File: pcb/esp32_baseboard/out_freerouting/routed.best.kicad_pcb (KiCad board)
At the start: 2 copper layers, 235 x 132 mm, 39 parts, among them J1 Screw_12V_IN, J10 LIM_HOME2, J12 LIM_HOME3, J14 BUP_30S, J15 BUZZER_5V, J16 AOD4184, J17 TFT_TOUCH, J18 EC11_ENC, J2 NEMA17_OUT, J5 28BYJ48, J6 28BYJ48, J7 28BYJ48, J8 LIM_HOME1, U1 ESP32_S3_DevKitC_1, U10 74HC595, U11 74HC595, U2 MP1584_5V3A, U3 TMC2209, U4 PC817_4CH, U5 ULN2003AN, U6 ULN2003AN, U7 ULN2003AN, U9 PC817_4CH_DNP

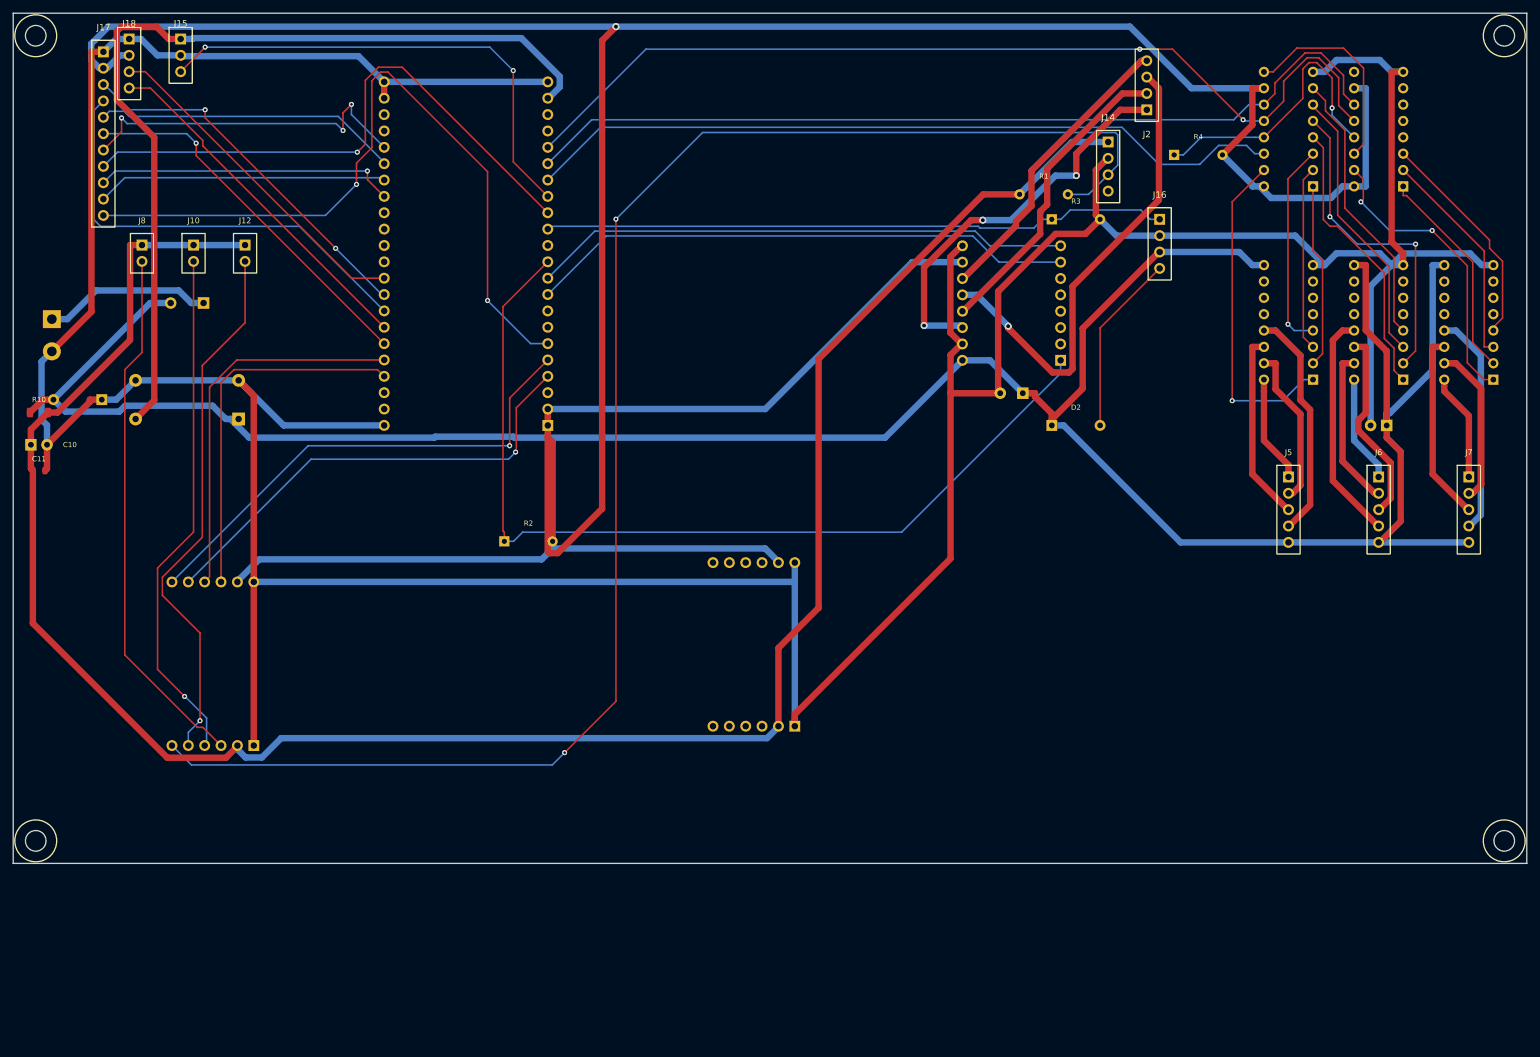
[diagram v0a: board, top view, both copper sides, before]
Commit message: đi dây cho mạch PCB
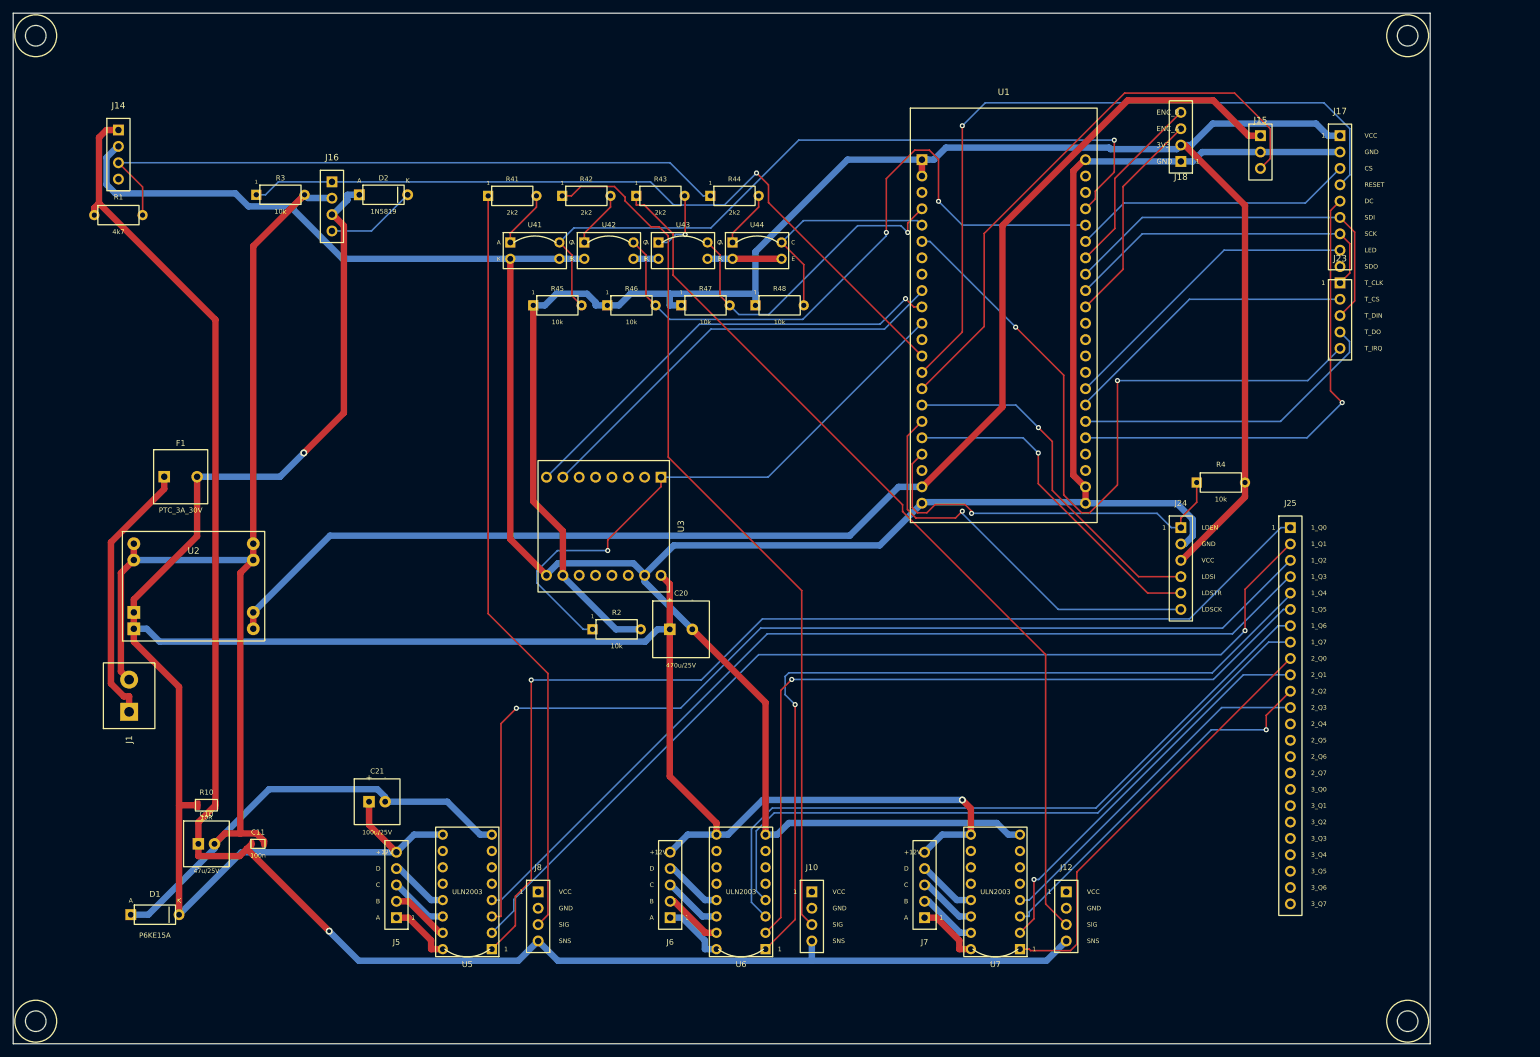
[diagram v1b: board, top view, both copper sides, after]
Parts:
- removed J2: NEMA17_OUT, ESP32_Carrier:PinHeader_1x04_Motor
- removed U10, U11: 74HC595, ESP32_Carrier:74HC595
- removed U4: PC817_4CH, ESP32_Carrier:PC817_4CH_Opto
- removed U9: PC817_4CH_DNP, ESP32_Carrier:PC817_4CH_Opto
- added J23: TFT_TP, ESP32_Carrier:PinHeader_1x05_TFT_TP, F.Cu at (241.0, 71.9)
- added J24: 595_CTRL, ESP32_Carrier:PinHeader_1x06_595CTRL, F.Cu at (216.3, 109.9)
- added J25: 595_Q, ESP32_Carrier:PinHeader_1x24_595Q, F.Cu at (233.3, 109.9)
- added R41: 2k2, ESP32_Carrier:R_Axial_4k7_BUP, F.Cu at (112.5, 58.4)
- added R42: 2k2, ESP32_Carrier:R_Axial_4k7_BUP, F.Cu at (124.0, 58.4)
- added R43: 2k2, ESP32_Carrier:R_Axial_4k7_BUP, F.Cu at (135.5, 58.4)
- added R44: 2k2, ESP32_Carrier:R_Axial_4k7_BUP, F.Cu at (147.0, 58.4)
- added R45: 10k, ESP32_Carrier:R_Axial_4k7_BUP, F.Cu at (119.5, 75.4)
- added R46: 10k, ESP32_Carrier:R_Axial_4k7_BUP, F.Cu at (131.0, 75.4)
- added R47: 10k, ESP32_Carrier:R_Axial_4k7_BUP, F.Cu at (142.5, 75.4)
- added R48: 10k, ESP32_Carrier:R_Axial_4k7_BUP, F.Cu at (154.0, 75.4)
- added U41: PC817, ESP32_Carrier:PC817_DIP4, F.Cu at (116.0, 66.9)
- added U42: PC817, ESP32_Carrier:PC817_DIP4, F.Cu at (127.5, 66.9)
- added U43: PC817, ESP32_Carrier:PC817_DIP4, F.Cu at (139.0, 66.9)
- added U44: PC817, ESP32_Carrier:PC817_DIP4, F.Cu at (150.5, 66.9)
- C20, C21, D1, F1, J1, U1, U2, U3, U5, U6, U7: moved to F.Cu
- J10: value LIM_HOME2 -> END_HOME2; footprint ESP32_Carrier:PinHeader_1x02_LimitSW -> ESP32_Carrier:PinHeader_1x04_Endstop
- J12: value LIM_HOME3 -> END_HOME3; footprint ESP32_Carrier:PinHeader_1x02_LimitSW -> ESP32_Carrier:PinHeader_1x04_Endstop
- J17: value TFT_TOUCH -> TFT_LCD; footprint ESP32_Carrier:PinHeader_1x11_TFT -> ESP32_Carrier:PinHeader_1x09_TFT_LCD
- J8: value LIM_HOME1 -> END_HOME1; footprint ESP32_Carrier:PinHeader_1x02_LimitSW -> ESP32_Carrier:PinHeader_1x04_Endstop
- moved J17 192.4 mm to (241.0, 49.0)
- moved J15 168.3 mm to (228.6, 49.0)
- moved C21 166.1 mm to (91.5, 152.4), turned to 0 degrees
- moved J18 164.4 mm to (216.3, 53.0), turned to 180 degrees
- moved J12 162.3 mm to (198.5, 166.4)
- moved U5 155.2 mm to (105.5, 166.4)
- moved J5 154.5 mm to (94.5, 170.4), turned to 180 degrees
- moved J14 153.7 mm to (51.3, 48.1)
- moved R1 143.7 mm to (51.3, 61.3)
- moved J10 138.9 mm to (159.0, 166.4)
- moved U6 132.7 mm to (148.0, 166.4)
- moved J6 129.5 mm to (137.0, 170.4), turned to 180 degrees
- moved J16 128.6 mm to (84.5, 56.2)
- moved R3 123.6 mm to (76.5, 58.2)
- moved J8 117.8 mm to (116.5, 166.4)
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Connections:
- J10 pad 1: +12V_SNS -> unconnected-(J10-VCC-Pad1)
- J10 pad 2: OPTO_IN2 -> unconnected-(J10-GND-Pad2)
- J12 pad 1: +12V_SNS -> unconnected-(J12-VCC-Pad1)
- J12 pad 2: OPTO_IN3 -> unconnected-(J12-GND-Pad2)
- J17 pad 1: GND -> +3V3
- J17 pad 2: +3V3 -> GND
- J17 pad 3: TFT_SCK -> TFT_CS
- J17 pad 4: TFT_MOSI -> TFT_RST
- J17 pad 5: TFT_MISO -> TFT_DC
- J17 pad 6: TFT_CS -> TFT_MOSI
- J17 pad 7: TFT_DC -> TFT_SCK
- J17 pad 8: TFT_RST -> TFT_BL
- J17 pad 9: TFT_BL -> unconnected-(J17-SDO-Pad9)
- J8 pad 1: +12V_SNS -> unconnected-(J8-VCC-Pad1)
- J8 pad 2: OPTO_IN1 -> unconnected-(J8-GND-Pad2)
- U2 pad 3: +5V -> GND
- U2 pad 4: GND -> +5V
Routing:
- net +3V3: track 542.4 -> 284.1 mm, vias 1 -> 0
- net OPTO_IN4: track 247.1 -> 103.7 mm, vias 2 -> 0
- net SR_Q2: track 28.7 -> 164.4 mm, vias 0 -> 1
- net SR_Q1: track 28.7 -> 153.8 mm, vias 0 -> 1
- net SR_Q0: track 51.8 -> 172.0 mm
- net SR_Q3: track 32.4 -> 144.8 mm, vias 1 -> 0
- net RCLK: track 148.6 -> 53.0 mm, vias 2 -> 1
- net SR_Q4: track 44.1 -> 128.8 mm, vias 0 -> 1
- net MotB1: track 74.2 -> 0.00 mm, vias 1 -> 0
- net SRCLK: track 138.3 -> 64.6 mm, vias 0 -> 1
- net SR_Q5: track 50.3 -> 122.9 mm, vias 2 -> 1
- net +5V: track 140.4 -> 210.6 mm
- net SR_Q6: track 43.4 -> 111.2 mm
- net SER: track 118.7 -> 55.7 mm, vias 0 -> 1
- net SR_Q7: track 43.4 -> 106.4 mm
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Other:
- board size 235 x 132 mm -> 220 x 160 mm
- board text added: "1: POWER J1+F1+D1+U2+RC"
- board text added: "2: MCU U1 ESP32-S3 DevKitC"
- board text added: "3: TMC U3 + Mot pins (NEMA17 on module)"
- board text added: "4: OPTO U41-U44 PC817 + R2k2/10k"
- board text added: "5: SHIFT U10 595-24IO + J24/J25 + R4"
- board text added: "A1: HOME1+U5+J5"
- board text added: "A2: HOME2+U6+J6"
- board text added: "A3: HOME3+U7+J7"
- board text added: "All parts TOP (F.Cu); B.Cu = routing only. Eco1 cluster = cyan"
- board text added: "B: BLOWER J16 AOD4184 + R3/D2"
- board text added: "C: HMI J17 LCD + J23 TP + J18 ENC + J15 BZ"
- board text added: "LCD"
- board text added: "OPTO PC817x8 + 2k2/10k"
- board text added: "R4 LDEN/OE pull-up 10k"
- board text added: "R41 LED HOME1"
- board text added: "R42 LED HOME2"
- board text added: "R43 LED HOME3"
- board text added: "R44 LED BUP"
- board text added: "R45 PU HOME1"
- board text added: "R46 PU HOME2"
- board text added: "R47 PU HOME3"
- board text added: "R48 PU BUP"
- board text added: "Shopee thegioimodule 3x595"
- board text added: "TP"
- board text added: "U10 74HC595-24IO module"
- board text added: "U: BUP-30S J14 + R1 4k7"
- board text removed: "1 POWER"
- board text removed: "2 MCU U1"
- board text removed: "3 TMC U3"
- board text removed: "5 U10/11 + U5-7"
- board text removed: "B STEP J2"
- board text removed: "BOTTOM — POWER | MCU | TMC | OPTO | 595/ULN"
- board text removed: "C HMI"
- board text removed: "E BYJ J5-J7"
- board text removed: "F HOME J8/10/12"
- board text removed: "G BLW"
- board text removed: "R4 OE_595 pull-up 10k"
- board text removed: "TOP 235x132 — ULN/595 + HOME + BYJ"
- board text removed: "U10 74HC595"
- board text removed: "U11 74HC595"
- board text removed: "U4 PC817 4CH"
- board text removed: "U4 used | U9 DNP spare"
- board text removed: "U5 ULN2003AN"
- board text removed: "U6 ULN2003AN"
- board text removed: "U7 ULN2003AN"
- board text removed: "U9 PC817 4CH DNP"
